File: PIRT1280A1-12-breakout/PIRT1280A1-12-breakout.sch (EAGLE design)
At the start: 12 parts, among them U1 PIRT1280A1-12

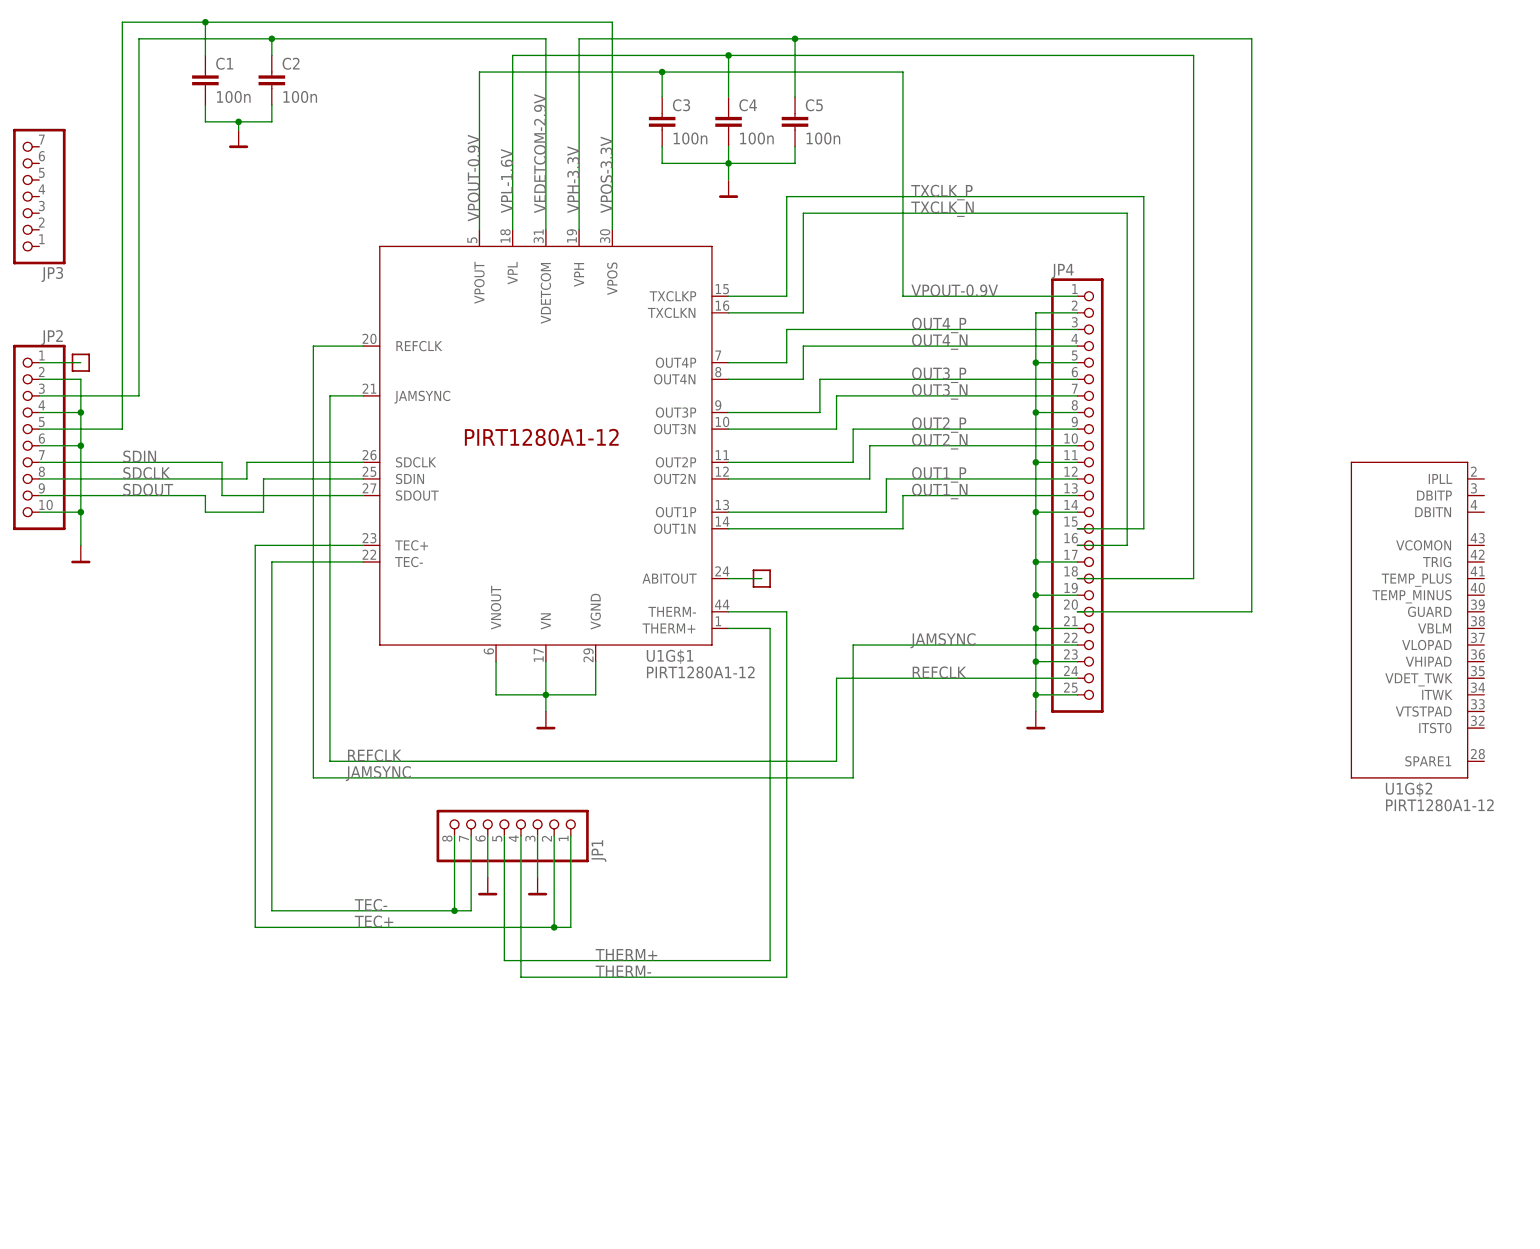
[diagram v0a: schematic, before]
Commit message: Mods from Oliver and Scott; more testpoints, stitching, ground points.
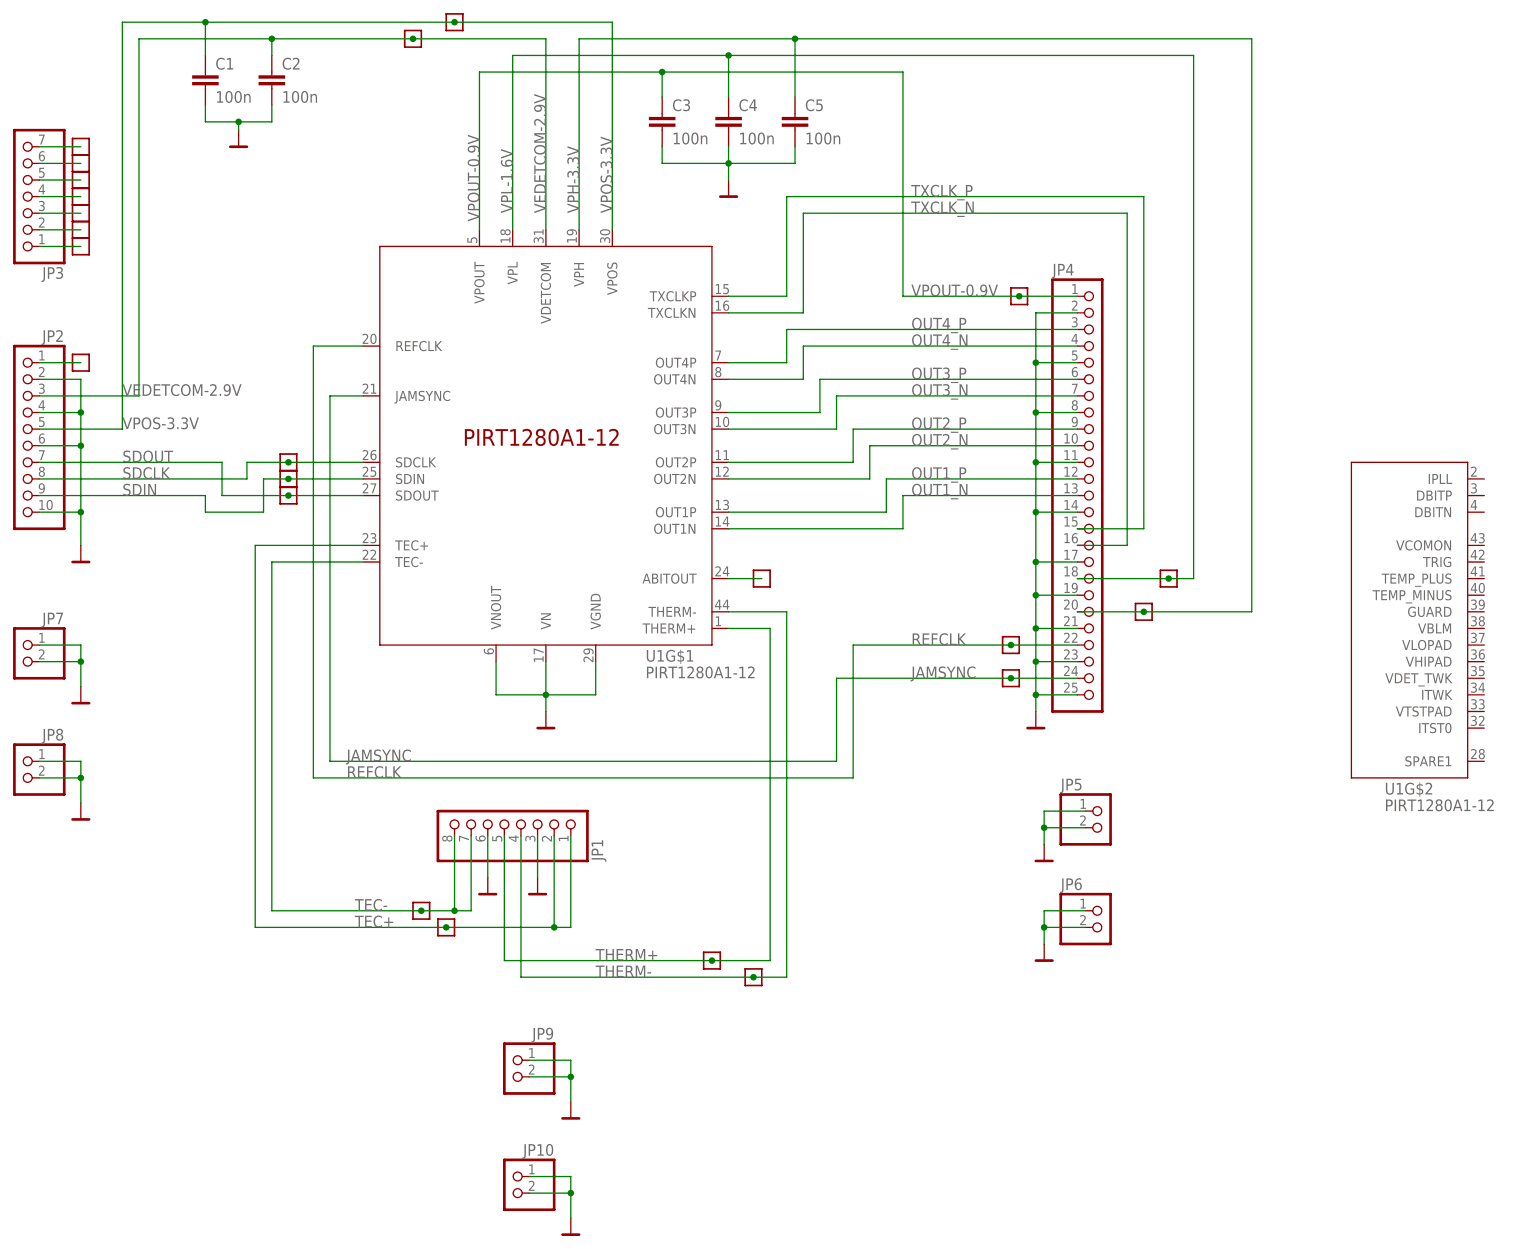
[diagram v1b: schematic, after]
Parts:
- added JP10, JP5, JP6, JP7, JP8, JP9: (no value), pinhead:PINHD-1X2
- added TP10, TP11, TP12, TP13, TP14, TP15, TP16, TP17, TP18, TP19, TP20, TP21, TP22, TP23, TP3, TP4, TP5, TP6, TP7, TP8, TP9: TEST-POINT-LARGE-SQUARE, oresat-misc:TEST-POINT-LARGE-SQUARE
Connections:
- net N$11 renamed ABITOUT
- new net N$2: JP3.7, TP9.1
- new net N$3: JP3.6, TP8.1
- new net N$4: JP3.5, TP7.1
- new net N$5: JP3.4, TP6.1
- new net N$6: JP3.3, TP5.1
- new net N$7: JP3.2, TP4.1
- new net N$8: JP3.1, TP3.1
- net GND: now also JP10.1, JP10.2, JP5.1, JP5.2, JP6.1, JP6.2, JP7.1, JP7.2, JP8.1, JP8.2, JP9.1, JP9.2
- net JAMSYNC: now also JP4.24, TP19.1, U1G$1.JAMSYNC; no longer JP4.22, U1G$1.REFCLK
- net REFCLK: now also JP4.22, TP20.1, U1G$1.REFCLK; no longer JP4.24, U1G$1.JAMSYNC
- net SDCLK: now also TP10.1
- net SDIN: now also JP2.9, TP11.1, U1G$1.SDIN; no longer JP2.7, U1G$1.SDOUT
- net SDOUT: now also JP2.7, TP12.1, U1G$1.SDOUT; no longer JP2.9, U1G$1.SDIN
- net TEC+: now also TP14.1
- net TEC-: now also TP13.1
- net THERM+: now also TP15.1
- net THERM-: now also TP16.1
- net VEDETCOM-2.9V: now also TP17.1
- net VPH-3.3V: now also TP21.1
- net VPL-1.6V: now also TP22.1
- net VPOS-3.3V: now also TP18.1
- net VPOUT-0.9V: now also TP23.1
